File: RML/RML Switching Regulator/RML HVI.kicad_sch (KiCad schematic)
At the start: 38 parts, among them Q1 Q_NMOS_GSD, Q2 Q_NMOS_GSD, U1 LM397, U2 HV9961LG-G, U3 74AHC1G02, U3 Optocoupler, U4 LM555xM, U5 LM1117DT-5.0

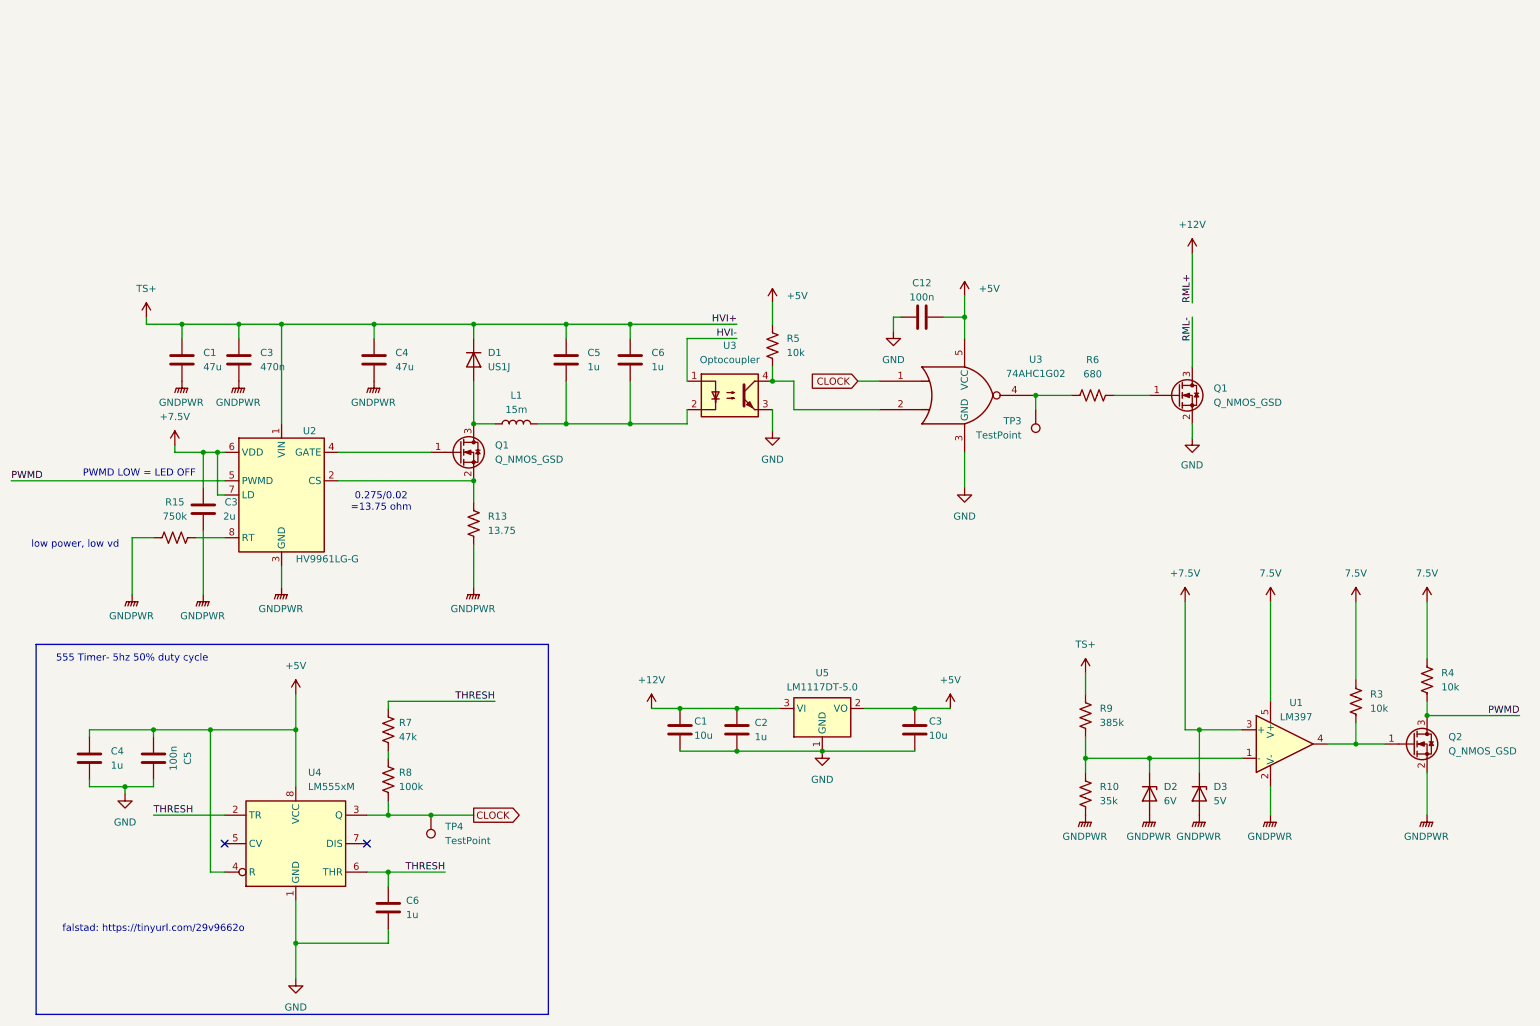
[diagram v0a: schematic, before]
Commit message: Added Remade RML and Safety Circuit
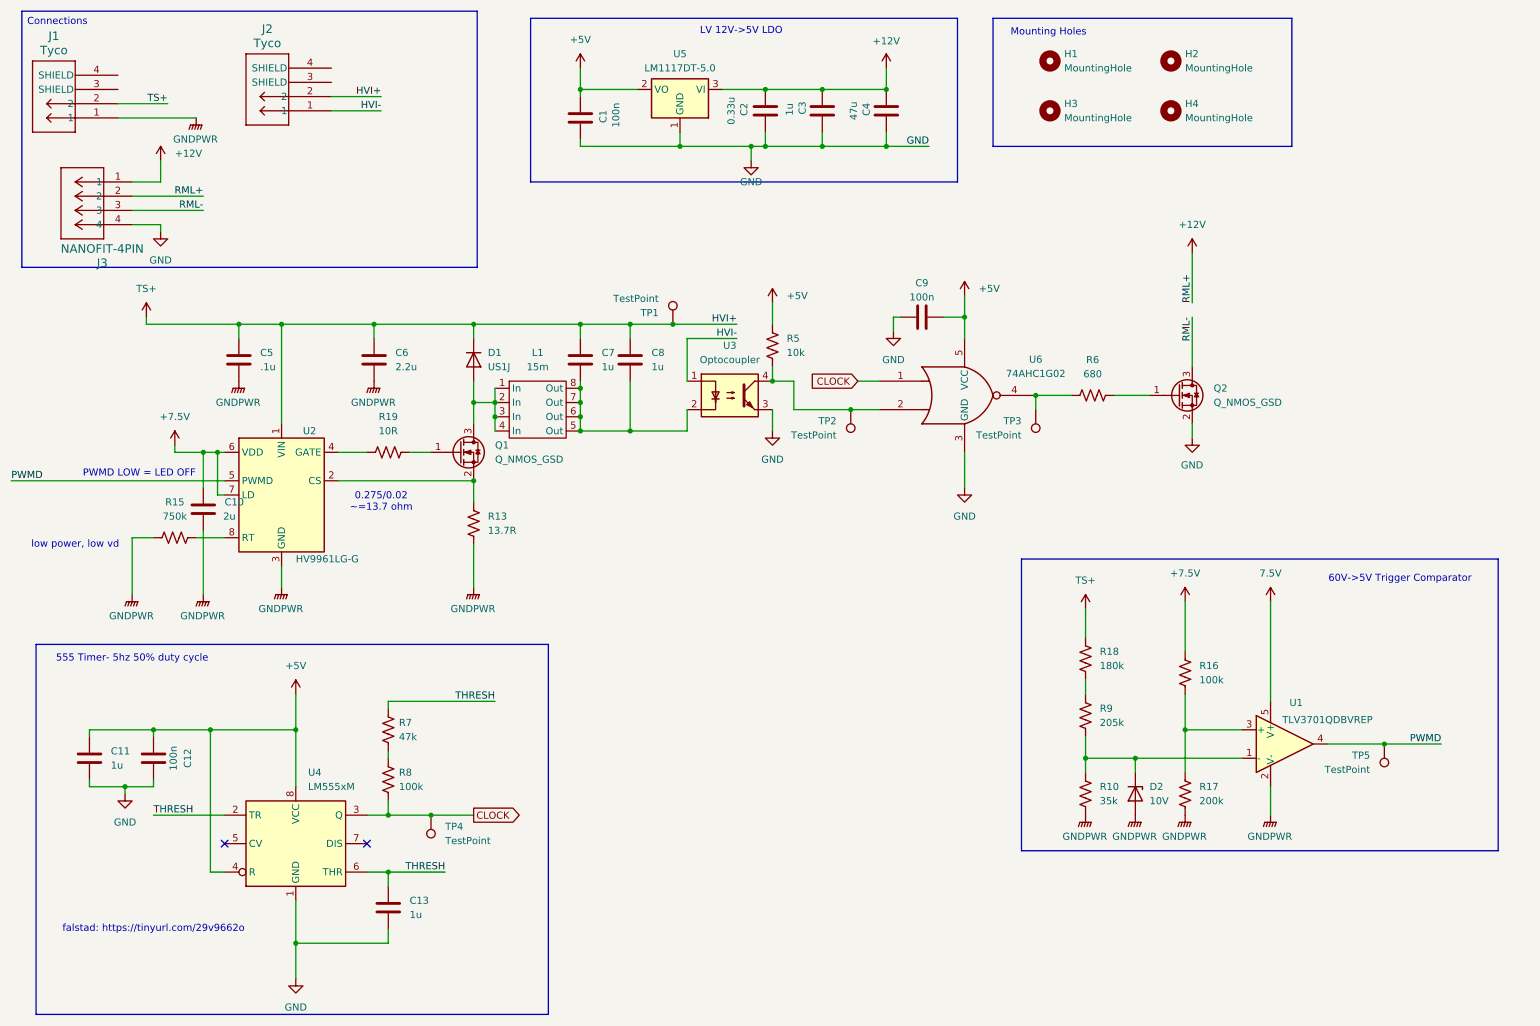
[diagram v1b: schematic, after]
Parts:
- removed C1: 47u, symbol Device:C
- removed C1: 10u, Capacitor_SMD:C_0603_1608Metric, symbol Device:C
- removed D3: 5V, symbol Device:D_Zener
- removed L1: 15m, symbol Device:L
- removed Q2: Q_NMOS_GSD, symbol Transistor_FET:Q_NMOS_GSD
- removed R3, R4: 10k, symbol Device:R_US
- added C1: 100n, Capacitor_SMD:C_0603_1608Metric_Pad1.08x0.95mm_HandSolder, symbol Device:C
- added C8: 1u, Capacitor_SMD:C_1210_3225Metric, symbol Device:C
- added H1, H2, H3, H4: MountingHole, MountingHole:MountingHole_3.2mm_M3_DIN965_Pad_TopOnly, symbol Mechanical:MountingHole
- added J1, J2: Tyco, Custom:tyco, symbol New_Library:Tyco
- added J3: NANOFIT-4PIN, Connector_Molex:Molex_Nano-Fit_105313-xx04_1x04_P2.50mm_Horizontal, symbol RML:MICROFIT-4PIN
- added L1: 15m, Custom:IND_BOURNS_SRR0908, symbol 1.Custom:8_pin_inductor
- added R16: 100k, Resistor_SMD:R_0805_2012Metric, symbol Device:R_US
- added R17: 200k, Resistor_SMD:R_0805_2012Metric, symbol Device:R_US
- added R18: 180k, Resistor_SMD:R_1210_3225Metric, symbol Device:R_US
- added R19: 10R, Resistor_SMD:R_0201_0603Metric, symbol Device:R_US
- added TP1, TP2, TP5: TestPoint, TestPoint:TestPoint_Pad_1.0x1.0mm, symbol Connector:TestPoint
- C10: renamed from C3; footprint (none) -> Capacitor_SMD:C_0805_2012Metric; Manufacture# (none) -> GXT21BR71C225KE01L; Mouser# (none) -> 81-GXT21BR71C225KE1L
- C2: value 1u -> 0.33u; footprint Capacitor_SMD:C_0603_1608Metric -> Capacitor_SMD:C_0603_1608Metric_Pad1.08x0.95mm_HandSolder; JLC# C1592 -> C282682
- C3: value 10u -> 1u; footprint Capacitor_SMD:C_0603_1608Metric -> Capacitor_SMD:C_0805_2012Metric_Pad1.18x1.45mm_HandSolder; JLC# C70225 -> C91186
- C4: footprint (none) -> Capacitor_SMD:CP_Elec_6.3x5.4; JLC# (none) -> C2836440
- C5: renamed from C3; value 470n -> .1u; footprint (none) -> Capacitor_SMD:C_1210_3225Metric; Manufacture# (none) -> C1210X104JCRAC3316; Mouser# (none) -> 80-C1210X104JCR3316
- C6: value 1u -> 2.2u; footprint (none) -> Custom:CAPC6050X550N; Manufacture# (none) -> CKG57NX7T2W225M500JH; Mouser# (none) -> 810-CKG57NX7T2W225M
- C7: renamed from C5; footprint (none) -> Capacitor_SMD:C_1210_3225Metric;  Manufacture# (none) -> KAF32GR71H105KU; Mouser# (none) -> 581-KAF32GR71H105KU
- D1: Manufacture (none) -> US1J; Mouser (none) -> 637-US1J
- D2: value 6V -> 10V; footprint (none) -> Diode_SMD:Nexperia_CFP3_SOD-123W; Manufacture# (none) -> MMSZ5240C-HE3_A-08; Mouser# (none) -> 78-MMSZ5240CHE3_A-08
- Q1: footprint (none) -> Package_TO_SOT_SMD:TO-252-3_TabPin2; Manufacture# (none) -> IPD70R1K4P7SAUMA1; Mouser# (none) -> 726-IPD70R1K4P7AUMA1
- R10: footprint (none) -> Resistor_SMD:R_0402_1005Metric; Manufacture# (none) -> RC0402FR-0735KL; Mouser# (none) -> 603-RC0402FR-0735KL
- R13: value 13.75 -> 13.7R; footprint (none) -> Resistor_SMD:R_0805_2012Metric; Manufacture# (none) -> RC0805FR-0713R7L; Mouser# (none) -> 603-RC0805FR-0713R7L
- R15: footprint (none) -> Resistor_SMD:R_0805_2012Metric
- R5: footprint Resistor_SMD:R_1206_3216Metric -> Resistor_SMD:R_0805_2012Metric; JLC# C1489 -> (none)
- R9: value 385k -> 205k; footprint (none) -> Resistor_SMD:R_1210_3225Metric; Manufacture# (none) -> AC1210FR-07205KL; Mouser# (none) -> 603-AC1210FR-07205KL
- U1: value LM397 -> TLV3701QDBVREP; JLC# C132076 -> (none); Manufacture# (none) -> TLV3701QDBVREP; Mouser# (none) -> 595-TLV3701QDBVREP
- U3: footprint (none) -> Custom:Q_Wurth_WL-OCPT_LSOP4-STANDARD; Manufacture# (none) -> VOLA617A-3X001T; Mouser# (none) -> 78-VOLA617A-3X001T
- U5: MOUSER (none) -> 926-LMC555CMX/NOPB
- renumbered C4 to C11, C5 to C12, C6 to C13, C12 to C9, Q1 to Q2, U3 to U6
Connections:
- net +12V: now also C3.1, C4.1, J3.1, J3.2
- net +5V: now also C1.2; no longer C3.1
- net +7.5V: now also R16.1; no longer U1.3 (+)
- net GND: now also C4.2, C1.1, J3.4
- net GNDPWR: now also C6.2, J1.1, R17.2; no longer C4.2
- net HVI-: now also J2.1
- net PWMD: now also U1.4, TP5.1
- net RML-: now also J3.3
- net TS+: now also C8.1, J1.2, J2.2, R18.1, TP1.1; no longer C4.1, R9.1
- net at C7.2, U3.2: now also C8.2, L1.5 (Out), L1.6 (Out), L1.7 (Out), L1.8 (Out); no longer C6.2
- net at Q1.1 (G): now also R19.2; no longer U2.4 (GATE)
- net at D1.2 (A), Q1.3 (D): now also L1.1 (In), L1.2 (In), L1.3 (In), L1.4 (In)
- net at R5.2, U3.4, U6.2: now also TP2.1
- new net: R16.2, R17.1, U1.3 (+)
- new net: R19.1, U2.4 (GATE)
- new net: R18.2, R9.1
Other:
- note added: "0.275/0.02 ~=13.7 ohm"
- note added: "60V->5V Trigger Comparator"
- note added: "LV 12V->5V LDO"
- note added: "Mounting Holes"
- note removed: "0.275/0.02 =13.75 ohm"
- moved on the sheet: C7, D2

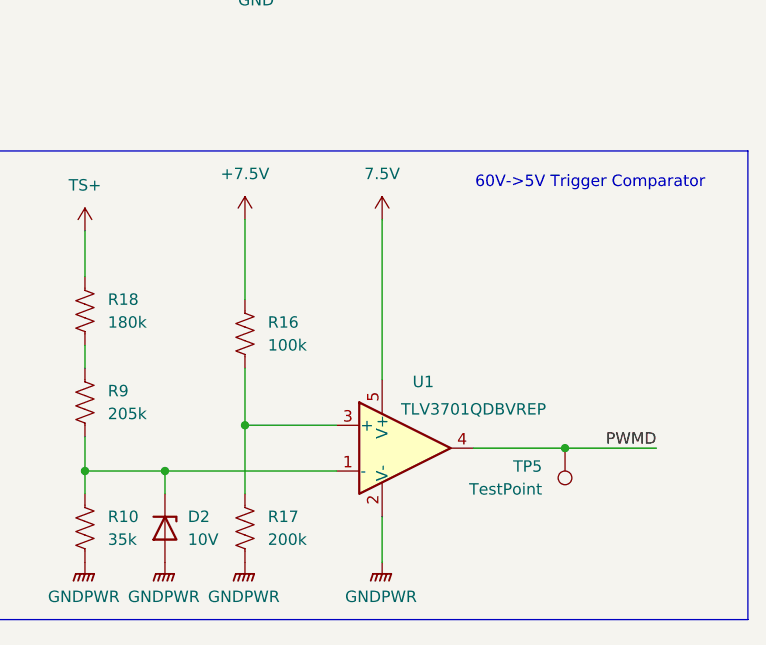
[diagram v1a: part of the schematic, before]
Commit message: Fixed Small Comparator issue on RML Switiching
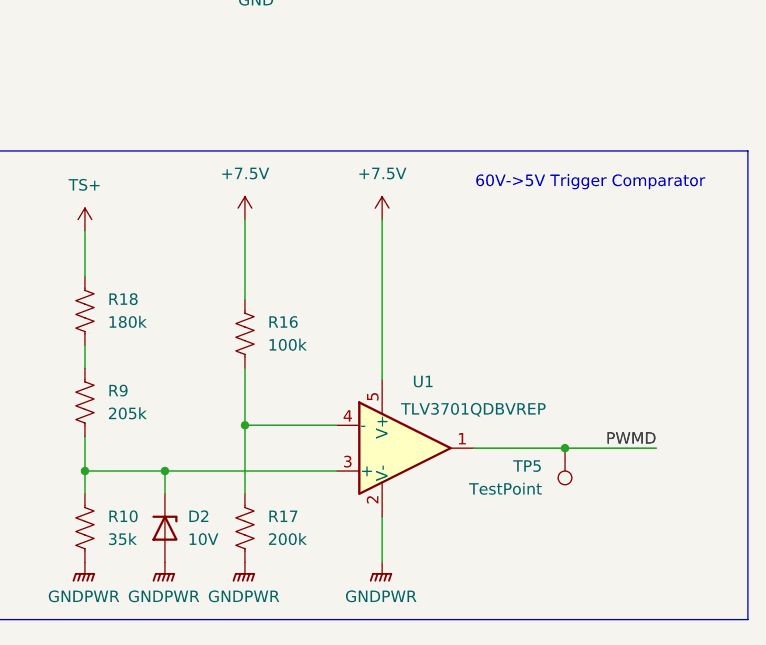
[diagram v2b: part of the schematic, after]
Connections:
- net 7.5V is gone; now on net +7.5V: U1.5 (V+)
- net PWMD: now also U1.1; no longer U1.4
- net at R16.2, R17.1: now also U1.4 (-); no longer U1.3 (+)
- net at D2.1 (K), R10.1, R9.2: now also U1.3 (+); no longer U1.1 (-)
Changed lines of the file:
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@@
 			)
 		)
-		(property "Value" "7.5V"
+		(property "Value" "+7.5V"
 			(at 237.49 115.57 0)
 			(effects
